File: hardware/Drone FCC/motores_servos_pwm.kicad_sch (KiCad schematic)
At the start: 26 parts, among them J301 ESC 1, J302 ESC 2, J303 ESC 3, J304 ESC 4, J305 ESC 5, J306 ESC 6, J307 ESC 7, J308 ESC 8, J309 SERVO 1, J310 SERVO 2, J311 SERVO 3, J312 SERVO 4, J313 Power Servo

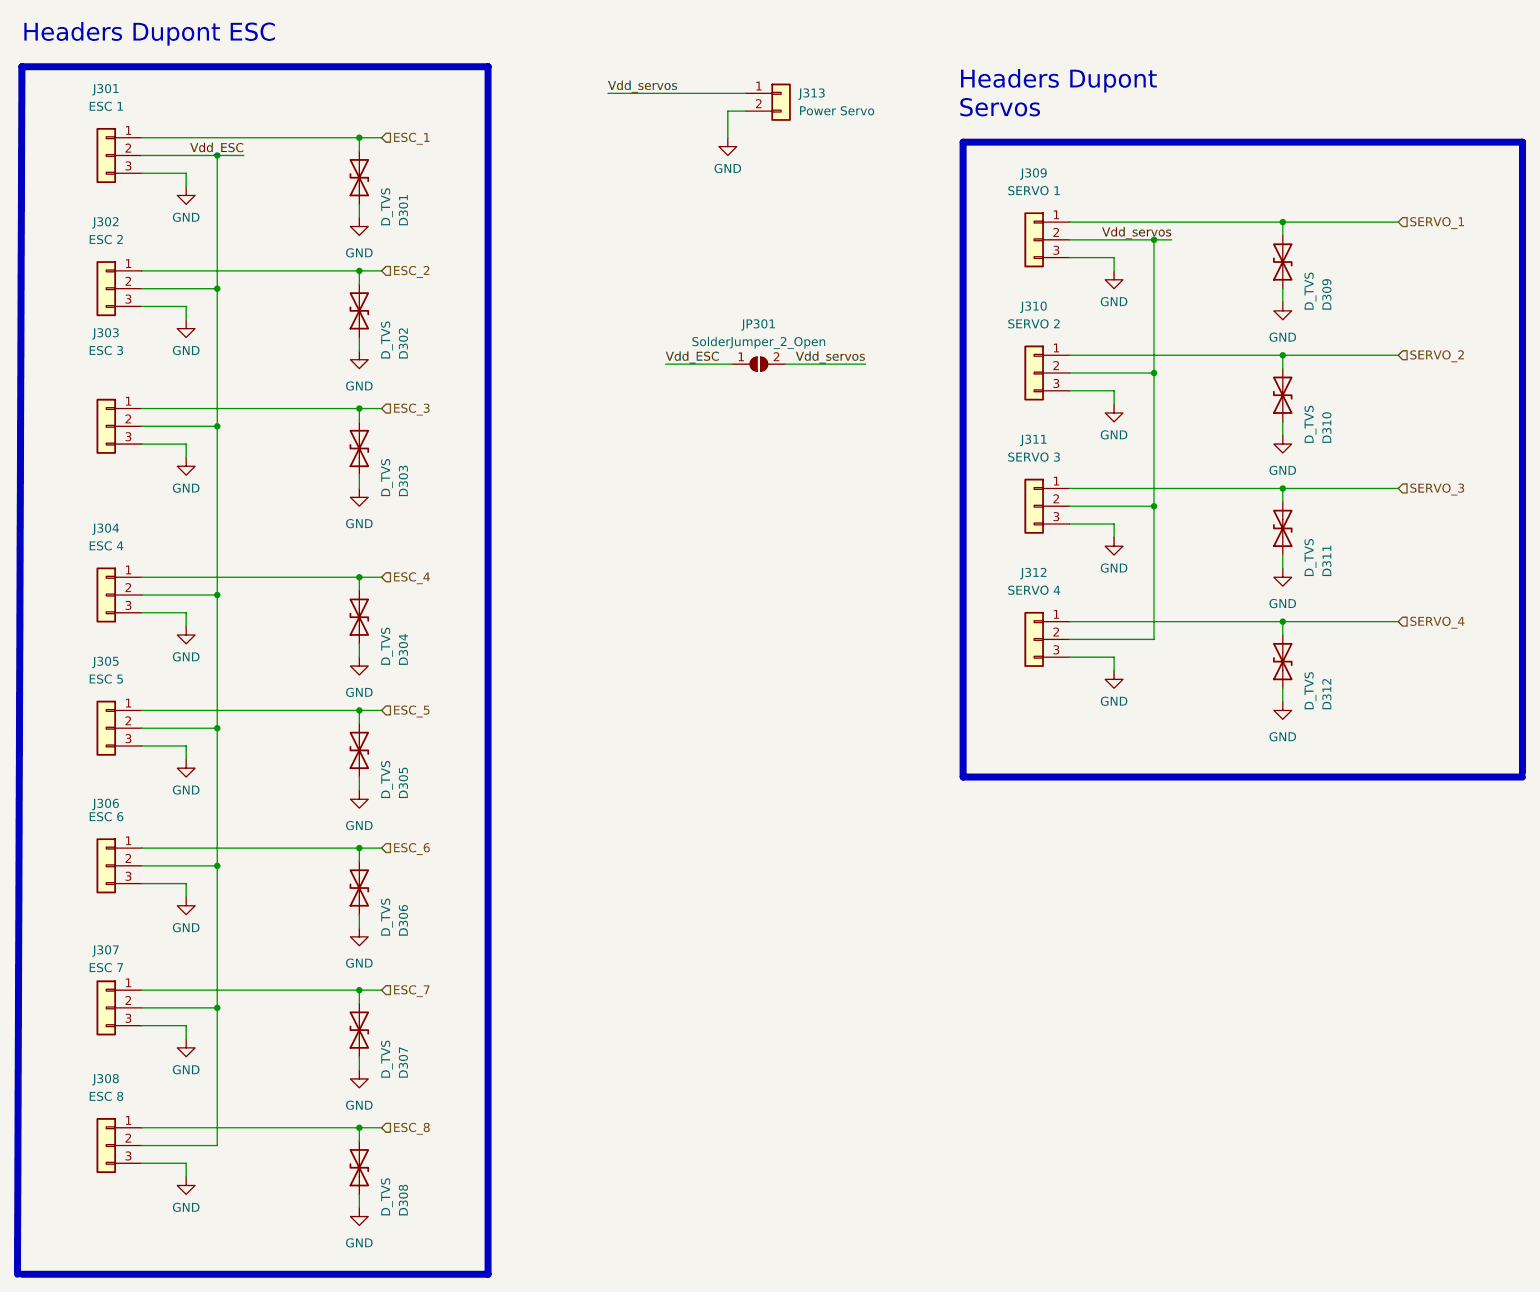
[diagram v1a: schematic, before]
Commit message: removed all the TVS from the PCB and SCH
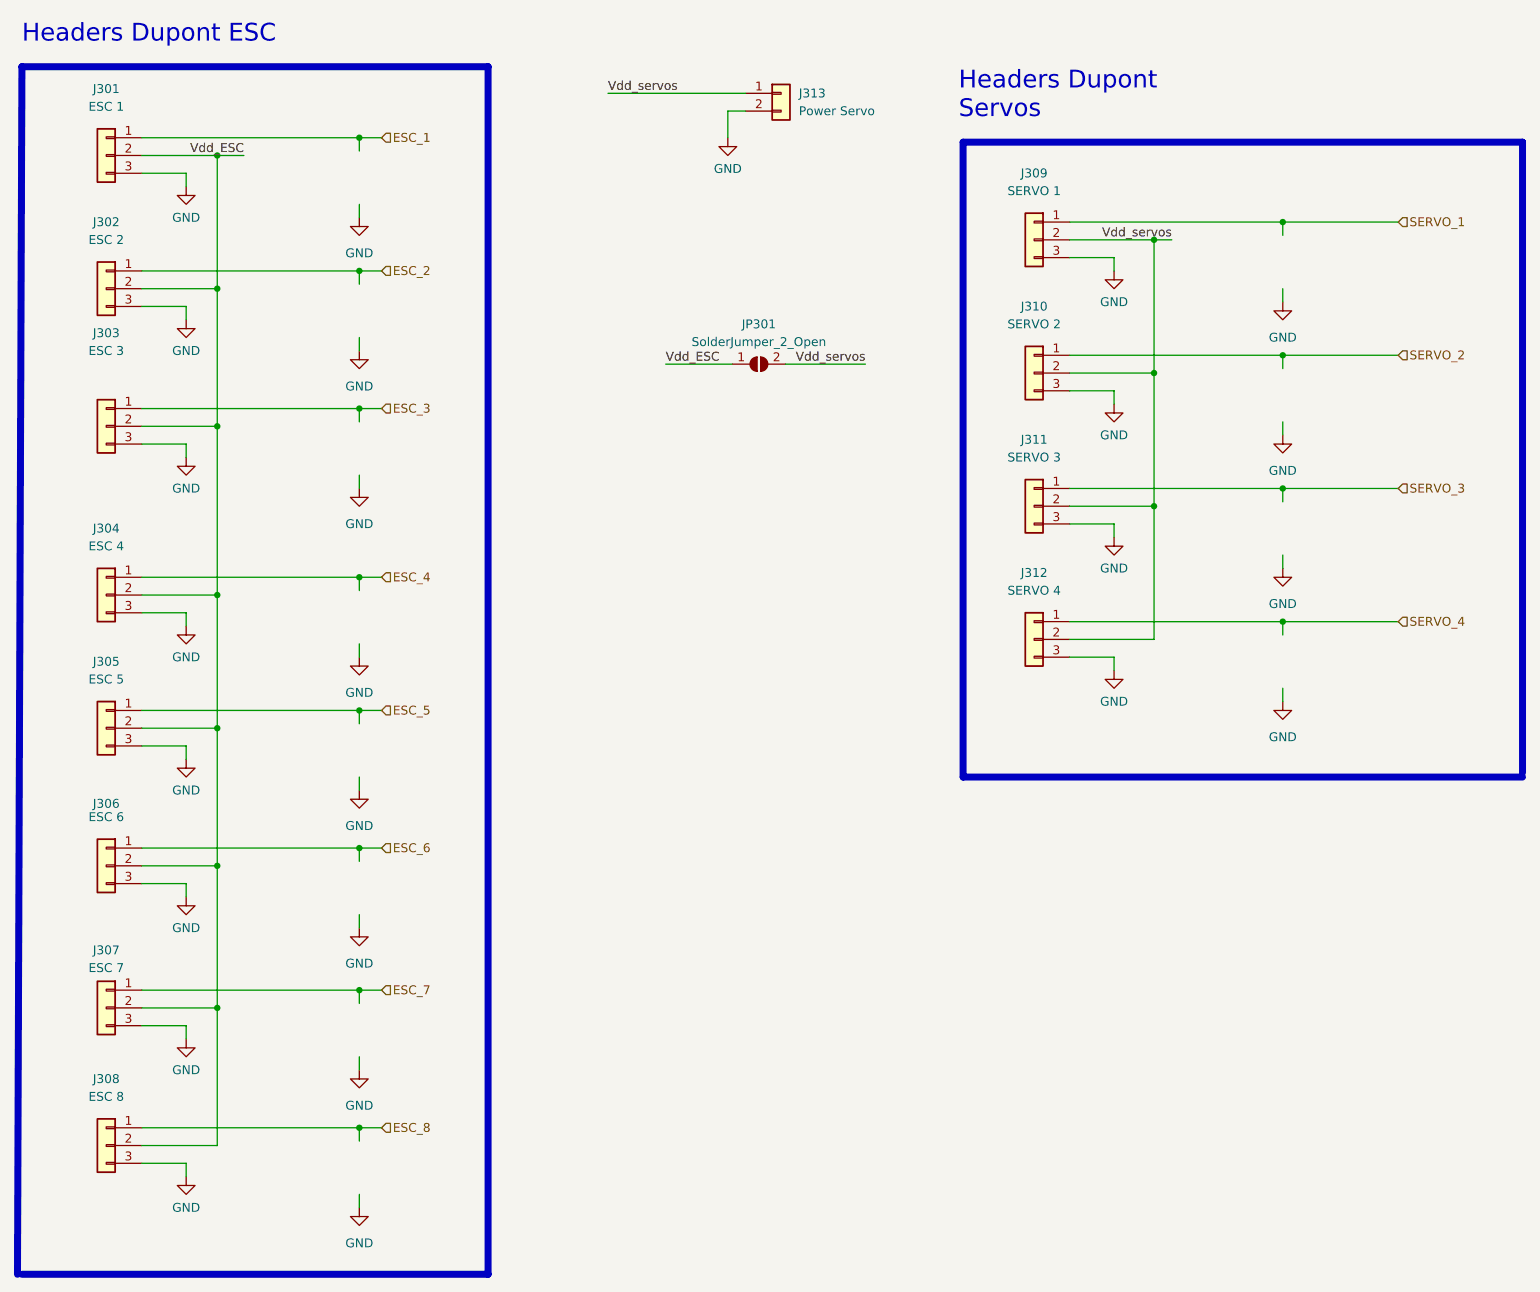
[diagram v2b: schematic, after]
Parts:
- removed D301, D302, D303, D304, D305, D306, D307, D308, D309, D310, D311, D312: D_TVS, Diode_SMD:D_0402_1005Metric_Pad0.77x0.64mm_HandSolder, symbol Device:D_TVS
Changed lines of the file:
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@@
     (pin "3")
-  )
-  (symbol (lib_id "Device:D_TVS") (at 104.775 179.07 90) (unit 1)
-    (in_bom yes) (on_board yes)
-    (property "Reference" "D308" (id 0) (at 111.125 186.055 0)
-      (effects (font (size 1.27 1.27)) (justify left))
-    )
-    (property "Value" "D_TVS" (id 1) (at 108.585 186.055 0)
-      (effects (font (size 1.27 1.27)) (justify left))
-    )
-    (property "Footprint" "Diode_SMD:D_0402_1005Metric_Pad0.77x0.64mm_HandSolder" (id 2) (at 104.775 179.07 0)
-      (effects (font (size 1.27 1.27)) hide)
-    )
-    (property "Datasheet" "~" (id 3) (at 104.775 179.07 0)
-      (effects (font (size 1.27 1.27)) hide)
-    )
-    (pin "1")
-    (pin "2")
   )
   (symbol (lib_id "power:GND") (at 104.775 81.915 0) (mirror y) (unit 1)
@@
     (pin "3")
   )
-  (symbol (lib_id "Device:D_TVS") (at 104.775 37.465 90) (unit 1)
-    (in_bom yes) (on_board yes)
-    (property "Reference" "D301" (id 0) (at 111.125 44.45 0)
-      (effects (font (size 1.27 1.27)) (justify left))
-    )
-    (property "Value" "D_TVS" (id 1) (at 108.585 44.45 0)
-      (effects (font (size 1.27 1.27)) (justify left))
-    )
-    (property "Footprint" "Diode_SMD:D_0402_1005Metric_Pad0.77x0.64mm_HandSolder" (id 2) (at 104.775 37.465 0)
-      (effects (font (size 1.27 1.27)) hide)
-    )
-    (property "Datasheet" "~" (id 3) (at 104.775 37.465 0)
-      (effects (font (size 1.27 1.27)) hide)
-    )
-    (pin "1")
-    (pin "2")
-  )
   (symbol (lib_id "power:GND") (at 236.855 112.395 0) (mirror y) (unit 1)
     (in_bom yes) (on_board yes) (fields_autoplaced)
@@
     (pin "1")
   )
-  (symbol (lib_id "Device:D_TVS") (at 236.855 106.68 90) (unit 1)
-    (in_bom yes) (on_board yes)
-    (property "Reference" "D312" (id 0) (at 243.205 113.665 0)
-      (effects (font (size 1.27 1.27)) (justify left))
-    )
-    (property "Value" "D_TVS" (id 1) (at 240.665 113.665 0)
-      (effects (font (size 1.27 1.27)) (justify left))
-    )
-    (property "Footprint" "Diode_SMD:D_0402_1005Metric_Pad0.77x0.64mm_HandSolder" (id 2) (at 236.855 106.68 0)
-      (effects (font (size 1.27 1.27)) hide)
-    )
-    (property "Datasheet" "~" (id 3) (at 236.855 106.68 0)
-      (effects (font (size 1.27 1.27)) hide)
-    )
-    (pin "1")
-    (pin "2")
-  )
   (symbol (lib_id "power:GND") (at 80.01 57.785 0) (unit 1)
     (in_bom yes) (on_board yes) (fields_autoplaced)
@@
     )
     (pin "1")
-  )
-  (symbol (lib_id "Device:D_TVS") (at 236.855 87.63 90) (unit 1)
-    (in_bom yes) (on_board yes)
-    (property "Reference" "D311" (id 0) (at 243.205 94.615 0)
-      (effects (font (size 1.27 1.27)) (justify left))
-    )
-    (property "Value" "D_TVS" (id 1) (at 240.665 94.615 0)
-      (effects (font (size 1.27 1.27)) (justify left))
-    )
-    (property "Footprint" "Diode_SMD:D_0402_1005Metric_Pad0.77x0.64mm_HandSolder" (id 2) (at 236.855 87.63 0)
-      (effects (font (size 1.27 1.27)) hide)
-    )
-    (property "Datasheet" "~" (id 3) (at 236.855 87.63 0)
-      (effects (font (size 1.27 1.27)) hide)
-    )
-    (pin "1")
-    (pin "2")
   )
   (symbol (lib_id "Connector_Generic:Conn_01x03") (at 68.58 53.34 0) (mirror y) (unit 1)
@@
     (pin "2")
     (pin "3")
-  )
-  (symbol (lib_id "Device:D_TVS") (at 104.775 100.33 90) (unit 1)
-    (in_bom yes) (on_board yes)
-    (property "Reference" "D304" (id 0) (at 111.125 107.315 0)
-      (effects (font (size 1.27 1.27)) (justify left))
-    )
-    (property "Value" "D_TVS" (id 1) (at 108.585 107.315 0)
-      (effects (font (size 1.27 1.27)) (justify left))
-    )
-    (property "Footprint" "Diode_SMD:D_0402_1005Metric_Pad0.77x0.64mm_HandSolder" (id 2) (at 104.775 100.33 0)
-      (effects (font (size 1.27 1.27)) hide)
-    )
-    (property "Datasheet" "~" (id 3) (at 104.775 100.33 0)
-      (effects (font (size 1.27 1.27)) hide)
-    )
-    (pin "1")
-    (pin "2")
-  )
-  (symbol (lib_id "Device:D_TVS") (at 236.855 68.58 90) (unit 1)
-    (in_bom yes) (on_board yes)
-    (property "Reference" "D310" (id 0) (at 243.205 75.565 0)
-      (effects (font (size 1.27 1.27)) (justify left))
-    )
-    (property "Value" "D_TVS" (id 1) (at 240.665 75.565 0)
-      (effects (font (size 1.27 1.27)) (justify left))
-    )
-    (property "Footprint" "Diode_SMD:D_0402_1005Metric_Pad0.77x0.64mm_HandSolder" (id 2) (at 236.855 68.58 0)
-      (effects (font (size 1.27 1.27)) hide)
-    )
-    (property "Datasheet" "~" (id 3) (at 236.855 68.58 0)
-      (effects (font (size 1.27 1.27)) hide)
-    )
-    (pin "1")
-    (pin "2")
   )
   (symbol (lib_id "Connector_Generic:Conn_01x03") (at 201.295 103.505 0) (mirror y) (unit 1)
@@
     (pin "3")
   )
-  (symbol (lib_id "Device:D_TVS") (at 104.775 139.065 90) (unit 1)
-    (in_bom yes) (on_board yes)
-    (property "Reference" "D306" (id 0) (at 111.125 146.05 0)
-      (effects (font (size 1.27 1.27)) (justify left))
-    )
-    (property "Value" "D_TVS" (id 1) (at 108.585 146.05 0)
-      (effects (font (size 1.27 1.27)) (justify left))
-    )
-    (property "Footprint" "Diode_SMD:D_0402_1005Metric_Pad0.77x0.64mm_HandSolder" (id 2) (at 104.775 139.065 0)
-      (effects (font (size 1.27 1.27)) hide)
-    )
-    (property "Datasheet" "~" (id 3) (at 104.775 139.065 0)
-      (effects (font (size 1.27 1.27)) hide)
-    )
-    (pin "1")
-    (pin "2")
-  )
-  (symbol (lib_id "Device:D_TVS") (at 104.775 159.385 90) (unit 1)
-    (in_bom yes) (on_board yes)
-    (property "Reference" "D307" (id 0) (at 111.125 166.37 0)
-      (effects (font (size 1.27 1.27)) (justify left))
-    )
-    (property "Value" "D_TVS" (id 1) (at 108.585 166.37 0)
-      (effects (font (size 1.27 1.27)) (justify left))
-    )
-    (property "Footprint" "Diode_SMD:D_0402_1005Metric_Pad0.77x0.64mm_HandSolder" (id 2) (at 104.775 159.385 0)
-      (effects (font (size 1.27 1.27)) hide)
-    )
-    (property "Datasheet" "~" (id 3) (at 104.775 159.385 0)
-      (effects (font (size 1.27 1.27)) hide)
-    )
-    (pin "1")
-    (pin "2")
-  )
   (symbol (lib_id "power:GND") (at 236.855 74.295 0) (mirror y) (unit 1)
     (in_bom yes) (on_board yes) (fields_autoplaced)
@@
     (pin "1")
   )
-  (symbol (lib_id "Device:D_TVS") (at 104.775 76.2 90) (unit 1)
-    (in_bom yes) (on_board yes)
-    (property "Reference" "D303" (id 0) (at 111.125 83.185 0)
-      (effects (font (size 1.27 1.27)) (justify left))
-    )
-    (property "Value" "D_TVS" (id 1) (at 108.585 83.185 0)
-      (effects (font (size 1.27 1.27)) (justify left))
-    )
-    (property "Footprint" "Diode_SMD:D_0402_1005Metric_Pad0.77x0.64mm_HandSolder" (id 2) (at 104.775 76.2 0)
-      (effects (font (size 1.27 1.27)) hide)
-    )
-    (property "Datasheet" "~" (id 3) (at 104.775 76.2 0)
-      (effects (font (size 1.27 1.27)) hide)
-    )
-    (pin "1")
-    (pin "2")
-  )
   (symbol (lib_id "Connector_Generic:Conn_01x03") (at 68.58 97.155 0) (mirror y) (unit 1)
     (in_bom yes) (on_board yes) (fields_autoplaced)
@@
     (pin "3")
   )
-  (symbol (lib_id "Device:D_TVS") (at 104.775 119.38 90) (unit 1)
-    (in_bom yes) (on_board yes)
-    (property "Reference" "D305" (id 0) (at 111.125 126.365 0)
-      (effects (font (size 1.27 1.27)) (justify left))
-    )
-    (property "Value" "D_TVS" (id 1) (at 108.585 126.365 0)
-      (effects (font (size 1.27 1.27)) (justify left))
-    )
-    (property "Footprint" "Diode_SMD:D_0402_1005Metric_Pad0.77x0.64mm_HandSolder" (id 2) (at 104.775 119.38 0)
-      (effects (font (size 1.27 1.27)) hide)
-    )
-    (property "Datasheet" "~" (id 3) (at 104.775 119.38 0)
-      (effects (font (size 1.27 1.27)) hide)
-    )
-    (pin "1")
-    (pin "2")
-  )
   (symbol (lib_id "power:GND") (at 80.01 180.34 0) (unit 1)
     (in_bom yes) (on_board yes) (fields_autoplaced)
@@
     (pin "3")
   )
-  (symbol (lib_id "Device:D_TVS") (at 104.775 56.515 90) (unit 1)
-    (in_bom yes) (on_board yes)
-    (property "Reference" "D302" (id 0) (at 111.125 63.5 0)
-      (effects (font (size 1.27 1.27)) (justify left))
-    )
-    (property "Value" "D_TVS" (id 1) (at 108.585 63.5 0)
-      (effects (font (size 1.27 1.27)) (justify left))
-    )
-    (property "Footprint" "Diode_SMD:D_0402_1005Metric_Pad0.77x0.64mm_HandSolder" (id 2) (at 104.775 56.515 0)
-      (effects (font (size 1.27 1.27)) hide)
-    )
-    (property "Datasheet" "~" (id 3) (at 104.775 56.515 0)
-      (effects (font (size 1.27 1.27)) hide)
-    )
-    (pin "1")
-    (pin "2")
-  )
   (symbol (lib_id "power:GND") (at 236.855 55.245 0) (mirror y) (unit 1)
     (in_bom yes) (on_board yes) (fields_autoplaced)
@@
     (pin "1")
   )
-  (symbol (lib_id "Device:D_TVS") (at 236.855 49.53 90) (unit 1)
-    (in_bom yes) (on_board yes)
-    (property "Reference" "D309" (id 0) (at 243.205 56.515 0)
-      (effects (font (size 1.27 1.27)) (justify left))
-    )
-    (property "Value" "D_TVS" (id 1) (at 240.665 56.515 0)
-      (effects (font (size 1.27 1.27)) (justify left))
-    )
-    (property "Footprint" "Diode_SMD:D_0402_1005Metric_Pad0.77x0.64mm_HandSolder" (id 2) (at 236.855 49.53 0)
-      (effects (font (size 1.27 1.27)) hide)
-    )
-    (property "Datasheet" "~" (id 3) (at 236.855 49.53 0)
-      (effects (font (size 1.27 1.27)) hide)
-    )
-    (pin "1")
-    (pin "2")
-  )
 )

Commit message: tidying up the schematic
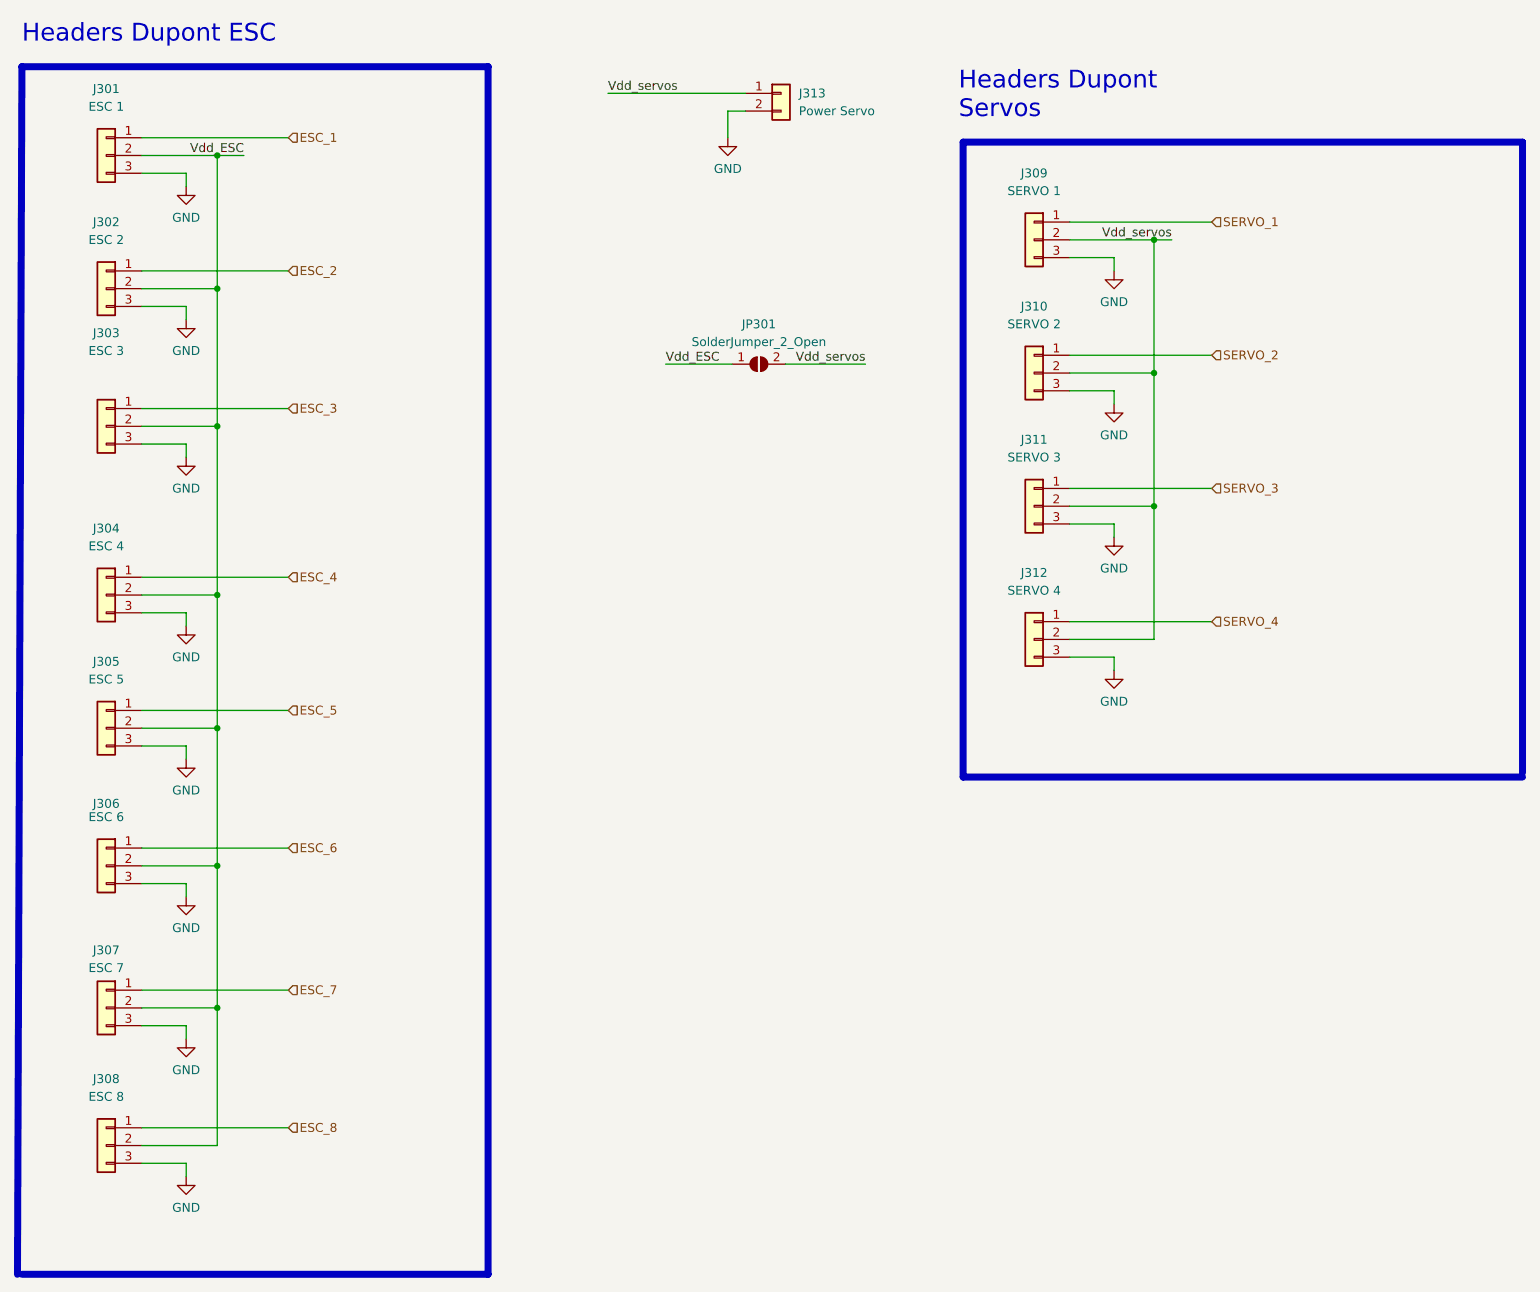
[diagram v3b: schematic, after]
